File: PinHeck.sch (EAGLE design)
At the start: 299 parts, among them IC1 FT232RQ, IC2 PIC32MX7X5FL-PT, IC3 CD74HCT244E, IC4 CD74HCT244E, IC5 ULN2803A, J1 500075-1517, J11 No Load, J2 500075-1517, J6 161-3507-E, SW1 101-0134-EV, SW2 101-0134-EV, U1 P8X32A-Q44, U10 74HCT2G04GV,125, U11 74HC165D,652, U12 74HC165D,652, U13 MIC1232, U14 MC74HC08ADG, U15 MC74HC08ADG, U16 MC74HC08ADG, U17 MC74HC08ADG, U18 MC74HC08ADG, U19 MC74HC08ADG, U2 FT230X, U20 TIP107, U21 TIP107, U22 TIP107, U23 TIP107, U24 TIP107, U25 TIP107, U26 TIP107, U27 TIP107, U28 TIP102, U29 TIP102, U3 74HC595D-Q100, U30 TIP102, U31 TIP102, U32 TIP102, U33 TIP102, U34 TIP102, U35 TIP102, U36 WS2801, U37 TIP102, U38 WS2801, U4 CAT24M01XI-T2, U5 74HC595D-Q100, U6 74HC595D-Q100, U7 74HC595D-Q100, U8 74HC595D-Q100, U9 74HC595D-Q100, X1 FQ7050B-8.000, X2 ECS-65-20-4X

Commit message: Changed the alphanumeric display to be GI.
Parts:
- removed AN_J3, AN_J6, AN_J7: 26-60-4090, PP_Connectors:PH_1X09MOLEX_KK_9
- removed C27, C28, C29, C30, C31: .1uF, PP_Passives:CAPACITOR_NON_POLAR0805
- removed MPU: (no value), PP_Connectors:PH_2X13HEADER_02X13_PTH
- added GI_0, GI_1: 26-60-4090, PP_Connectors:PH_1X09MOLEX_KK_9
- added R101, R103, R105, R107, R109, R111, R113, R125, R126, R127, R128, R129, R130, R131, R132, R99: 360, PP_Passives:RESISTOR0805
- added U40, U41, U42, U43, U44, U45, U46, U47, U48, U49, U50, U51: TIP102, PP_DiscreteSemi:BJT_NPN_SINGLETO-220
- SOL_0, SOL_1, SOL_10, SOL_11, SOL_12, SOL_13, SOL_14, SOL_15, SOL_16, SOL_17, SOL_18, SOL_19, SOL_2, SOL_20, SOL_21, SOL_22, SOL_23, SOL_3, SOL_4, SOL_5, SOL_6, SOL_7, SOL_8, SOL_9: value RFP12N10L -> IRL530
- U6, U7, U8, U9: value 74HC595D-Q100 -> TIP102; device PP_DigitalIC:74HC595SO-16 -> PP_DiscreteSemi:BJT_NPN_SINGLETO-220
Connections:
- net AN_DATA_COL renamed GI_DATA_COL
- net AN_DATA_COL_B renamed GI_DATA_COL_B
- removed net AN_J3_1: AN_J3.1, U5.Q7
- removed net AN_J3_2: AN_J3.2, U5.Q6
- removed net AN_J3_3: AN_J3.3, U5.Q5
- removed net AN_J3_4: AN_J3.4, U5.Q4
- removed net AN_J3_5: AN_J3.5, U5.Q3
- removed net AN_J3_6: AN_J3.6, U5.Q2
- removed net AN_J3_7: AN_J3.8, U5.Q1
- removed net AN_J3_8: AN_J3.9, U5.Q0
- removed net AN_J6_1: AN_J6.1, U3.Q7
- removed net AN_J6_2: AN_J6.2, U3.Q6
- removed net AN_J6_3: AN_J6.3, U3.Q5
- removed net AN_J6_4: AN_J6.4, U3.Q4
- removed net AN_J6_5: AN_J6.5, U3.Q3
- removed net AN_J6_6: AN_J6.6, U3.Q2
- removed net AN_J6_7: AN_J6.7, U3.Q1
- removed net AN_J6_8: AN_J6.9, U3.Q0
- removed net AN_J7_1: AN_J7.1, U6.Q0
- removed net AN_J7_2: AN_J7.2, U6.Q1
- removed net AN_J7_3: AN_J7.3, U6.Q2
- removed net AN_J7_4: AN_J7.4, U6.Q3
- removed net AN_J7_5: AN_J7.5, U6.Q4
- removed net AN_J7_6: AN_J7.7, U6.Q5
- removed net AN_J7_7: AN_J7.8, U6.Q6
- removed net AN_J7_8: AN_J7.9, U6.Q7
- removed net MPU_10: MPU.10, U7.Q0
- removed net MPU_11: MPU.11, U9.Q7
- removed net MPU_12: MPU.12, U9.Q6
- removed net MPU_13: MPU.13, U9.Q5
- removed net MPU_14: MPU.14, U9.Q4
- removed net MPU_15: MPU.15, U9.Q3
- removed net MPU_16: MPU.16, U9.Q2
- removed net MPU_17: MPU.17, U9.Q1
- removed net MPU_18: MPU.18, U9.Q0
- removed net MPU_19: MPU.19, U8.Q7
- removed net MPU_20: MPU.20, U8.Q6
- removed net MPU_21: MPU.21, U8.Q5
- removed net MPU_22: MPU.22, U8.Q4
- removed net MPU_23: MPU.23, U8.Q3
- removed net MPU_24: MPU.24, U8.Q2
- removed net MPU_25: MPU.25, U8.Q1
- removed net MPU_26: MPU.26, U8.Q0
- removed net MPU_3: MPU.3, U7.Q7
- removed net MPU_4: MPU.4, U7.Q6
- removed net MPU_5: MPU.5, U7.Q5
- removed net MPU_6: MPU.6, U7.Q4
- removed net MPU_7: MPU.7, U7.Q3
- removed net MPU_8: MPU.8, U7.Q2
- removed net MPU_9: MPU.9, U7.Q1
- removed net ROW_ONE_DATE_B: U8.Q7S, U9.DS
- removed net ROW_ZERO_DATA_B: U6.Q7S, U7.DS
- new net GI_0: R99.1, U3.Q0
- new net GI_1: R101.1, U3.Q1
- new net GI_10: R127.1, U5.Q2
- new net GI_11: R128.1, U5.Q3
- new net GI_12: R129.1, U5.Q4
- new net GI_13: R130.1, U5.Q5
- new net GI_14: R131.1, U5.Q6
- new net GI_15: R132.1, U5.Q7
- new net GI_2: R103.1, U3.Q2
- new net GI_3: R105.1, U3.Q3
- new net GI_4: R107.1, U3.Q4
- new net GI_5: R109.1, U3.Q5
- new net GI_6: R111.1, U3.Q6
- new net GI_7: R113.1, U3.Q7
- new net GI_8: R125.1, U5.Q0
- new net GI_9: R126.1, U5.Q1
- new net GI_R_0: GI_0.1, U6.COLLECTOR
- new net GI_R_1: GI_0.2, U7.COLLECTOR
- new net GI_R_10: GI_1.3, U46.COLLECTOR
- new net GI_R_11: GI_1.4, U47.COLLECTOR
- new net GI_R_12: GI_1.5, U48.COLLECTOR
- new net GI_R_13: GI_1.6, U49.COLLECTOR
- new net GI_R_14: GI_1.7, U50.COLLECTOR
- new net GI_R_15: GI_1.8, U51.COLLECTOR
- new net GI_R_2: GI_0.3, U8.COLLECTOR
- new net GI_R_3: GI_0.4, U9.COLLECTOR
- new net GI_R_4: GI_0.5, U40.COLLECTOR
- new net GI_R_5: GI_0.6, U41.COLLECTOR
- new net GI_R_6: GI_0.7, U42.COLLECTOR
- new net GI_R_7: GI_0.8, U43.COLLECTOR
- new net GI_R_8: GI_1.1, U44.COLLECTOR
- new net GI_R_9: GI_1.2, U45.COLLECTOR
- new net N$481: R99.2, U6.BASE
- new net N$482: R101.2, U7.BASE
- new net N$483: R103.2, U8.BASE
- new net N$484: R105.2, U9.BASE
- new net N$485: R107.2, U40.BASE
- new net N$486: R109.2, U41.BASE
- new net N$487: R111.2, U42.BASE
- new net N$488: R113.2, U43.BASE
- new net N$489: R125.2, U44.BASE
- new net N$490: R126.2, U45.BASE
- new net N$491: R127.2, U46.BASE
- new net N$492: R128.2, U47.BASE
- new net N$493: R129.2, U48.BASE
- new net N$494: R130.2, U49.BASE
- new net N$495: R131.2, U50.BASE
- new net N$496: R132.2, U51.BASE
- net !AN_BLANK: no longer MPU.1
- net !DATA_LAT: no longer U6.SHCP, U7.SHCP, U8.SHCP, U9.SHCP
- net 5V: now also GI_0.9, GI_1.9; no longer C27.2, C28.2, C29.2, C30.2, C31.2, U6.MR, U6.VCC, U7.MR, U7.VCC, U8.GND, U8.MR, U8.VCC, U9.MR, U9.VCC
- net DATA_CLK: no longer U6.STCP, U7.STCP, U8.STCP, U9.STCP
- net GND: now also U40.EMITTER, U41.EMITTER, U42.EMITTER, U43.EMITTER, U44.EMITTER, U45.EMITTER, U46.EMITTER, U47.EMITTER, U48.EMITTER, U49.EMITTER, U50.EMITTER, U51.EMITTER, U6.EMITTER, U7.EMITTER, U8.EMITTER, U9.EMITTER; no longer C27.1, C28.1, C29.1, C30.1, C31.1, IC5.CD+, MPU.2, U6.GND, U6.OE, U7.GND, U7.OE, U8.OE, U9.GND, U9.OE
- net ROW_ONE_DATA: no longer U8.DS
- net ROW_ZERO_DATA: no longer U6.DS
- net S_L: now also J6.R; no longer J6.T
- net S_R: now also J6.T; no longer J6.R
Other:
- moved on the sheet: C25, C26, J6

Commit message: Changed Watchdog timer to work via 555timer
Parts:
- removed C49: .1uF, PP_Passives:CAPACITOR_NON_POLAR0805
- removed U13: MIC1232, PP_FreqCtrl:MIC1232MYSOIC-8
- added C27: EEE-1VA101XP, PP_Passives:CAPACITOR_POLARIZED6.3MM_SMD
- added D2: (no value), PP_Passives:DIODESOD-128
- added P1: TC33X-2-103E, PP_Passives:TC33X-1TC33X-1
- added R133, R135: 10K, PP_Passives:RESISTOR0805
- added R134: 20K, PP_Passives:RESISTOR0805
- added U52: CD74HC123M96, PP_DigitalIC:74HC123SOIC-16
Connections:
- new net N$497: P1.2_WIPER, R134.1
- new net WATCHDOG_ADJUST: C27.POS, D2.ANODE, P1.3_CW, U52.1RXCX
- net 5V: now also D2.CATHODE, R134.2, U52.!1B, U52.!1R, U52.VCC; no longer C49.1, U13.TD, U13.TOL, U13.VCC
- net GND: now also C27.NEG, R133.2, R135.2, U52.1CX, U52.GND; no longer C49.2, U13.GND
- net PIC_ENABLE: now also R133.1, U52.!1A; no longer U13./ST
- net S_L: now also J6.T; no longer J6.R
- net S_R: now also J6.R; no longer J6.T
- net WATCHDOG: now also R135.1, U52.1Q; no longer U13./RST
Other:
- moved on the sheet: C48, J6, R118, WATCHDOG

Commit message: Fixing some layout issues. Added some breakouts.
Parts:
- added J3: (no value), PP_Connectors:PH_1X04HEADER_PTH
- added R136: 0, PP_Passives:RESISTOR0805
- D2: value (none) -> CGRM4001-HF; device PP_Passives:DIODESOD-128 -> PP_Passives:DIODESOD-123
- renumbered SUPER_AUX_CON to TCBTWDN
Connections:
- net !AN_BLANK: now also J3.4
- net GND: now also J3.2, J3.3, R136.1
- net SOL_GND: now also R136.2
- net WATCHDOG: now also J3.1

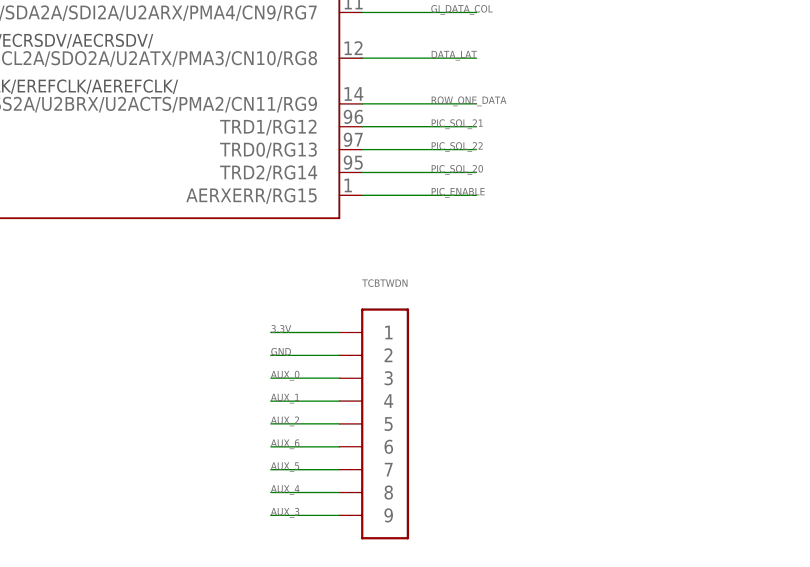
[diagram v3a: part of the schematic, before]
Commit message: changed port name. added new layout pic.
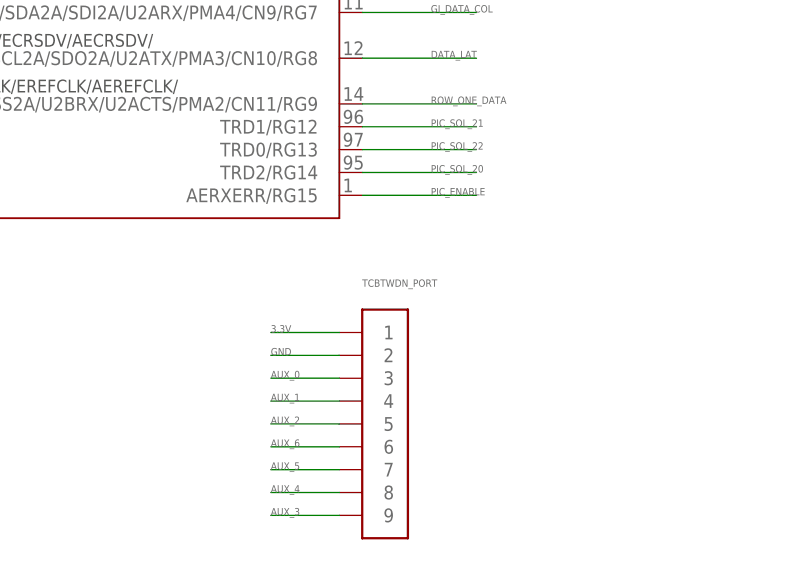
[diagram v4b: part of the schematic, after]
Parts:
- renumbered TCBTWDN to TCBTWDN_PORT

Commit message: New Spooky Logo
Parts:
- added LOGO1: SPOOKY_LOGOSPOOKY_LOGO, PP_Aesthetics:SPOOKY_LOGOSPOOKY_LOGO
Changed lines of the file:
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@@
 <part name="J3" library="PP_Connectors" deviceset="PH_1X04" device="HEADER_PTH"/>
 <part name="R136" library="PP_Passives" deviceset="RESISTOR" device="0805" value="0"/>
+<part name="LOGO1" library="PP_Aesthetics" deviceset="SPOOKY_LOGO" device="SPOOKY_LOGO"/>
 </parts>
 <sheets>
@@
 <instance part="J3" gate="G$1" x="530.86" y="40.64"/>
 <instance part="R136" gate="G$1" x="721.36" y="58.42" rot="MR0"/>
+<instance part="LOGO1" gate="G$1" x="-99.06" y="190.5"/>
 </instances>
 <busses>

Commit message: Fixed Bill of Material Issues
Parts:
- AUX_PORT, CABINET: value (none) -> 26-60-4120
- BOARD_POWER, SOL_PWR: value (none) -> 26-62-4040
- C34, C38, C42, C50: value 100uF -> EEE-1VA101XP
- D1: value BAV99W -> BAV99W,115
- D8: value NSQA6V8 -> NSQA6V8AW5T2G
- DMD_CON: value (none) -> 1-1634688-4
- DMD_PWR: value (none) -> 26-60-4020
- F1, F2, F3: value (none) -> 4245K
- IC1: value FT232RQ -> FT232RQ-REEL
- J3, TCBTWDN_PORT: value (none) -> N/A
- KNOCKER: value (none) -> 26-64-4030
- LIGHT_COL, LIGHT_ROW, SOL_BANK_0, SOL_BANK_1, SOL_BANK_2, SW_COL, SW_ROW: value (none) -> 26-64-4100
- PIC_RX, PIC_TX, PIC_USB, PROP_ACT, PROP_RX, PROP_TX, PROP_USB, PSU_PWR, WATCHDOG: value (none) -> VLMG1500-GS08
- RGB_CONN: value (none) -> 26-60-4080
- SOL_0, SOL_1, SOL_10, SOL_11, SOL_12, SOL_13, SOL_14, SOL_15, SOL_16, SOL_17, SOL_18, SOL_19, SOL_2, SOL_20, SOL_21, SOL_22, SOL_23, SOL_3, SOL_4, SOL_5, SOL_6, SOL_7, SOL_8, SOL_9: value IRL530 -> IRL530PBF
- U2: value FT230X -> FT230XS-R
- U39: value (none) -> LM2937IMP-3.3/NOPB
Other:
- moved on the sheet: DMD_CON

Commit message: Fixed Part Names
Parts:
- IC2: value PIC32MX7X5FL-PT -> PIC32MX795F512L-80I/PT
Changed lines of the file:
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@@
 <parts>
 <part name="IC1" library="IC" deviceset="FT232R" device="L" value="FT232RQ-REEL"/>
-<part name="IC2" library="Microchip" deviceset="PIC32MX7X5F*L" device="-PT"/>
+<part name="IC2" library="Microchip" deviceset="PIC32MX7X5F*L" device="-PT" value="PIC32MX795F512L-80I/PT"/>
 <part name="D1" library="Discrete" deviceset="BAV99W" device="" value="BAV99W,115"/>
 <part name="J11" library="Mechanical" deviceset="HDR-1X6-OFFSET" device="" value="No Load"/>
